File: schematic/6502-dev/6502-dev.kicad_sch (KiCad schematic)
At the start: 10 parts, among them SW1 SW_Push, U1 NE555P, U2 74HC02

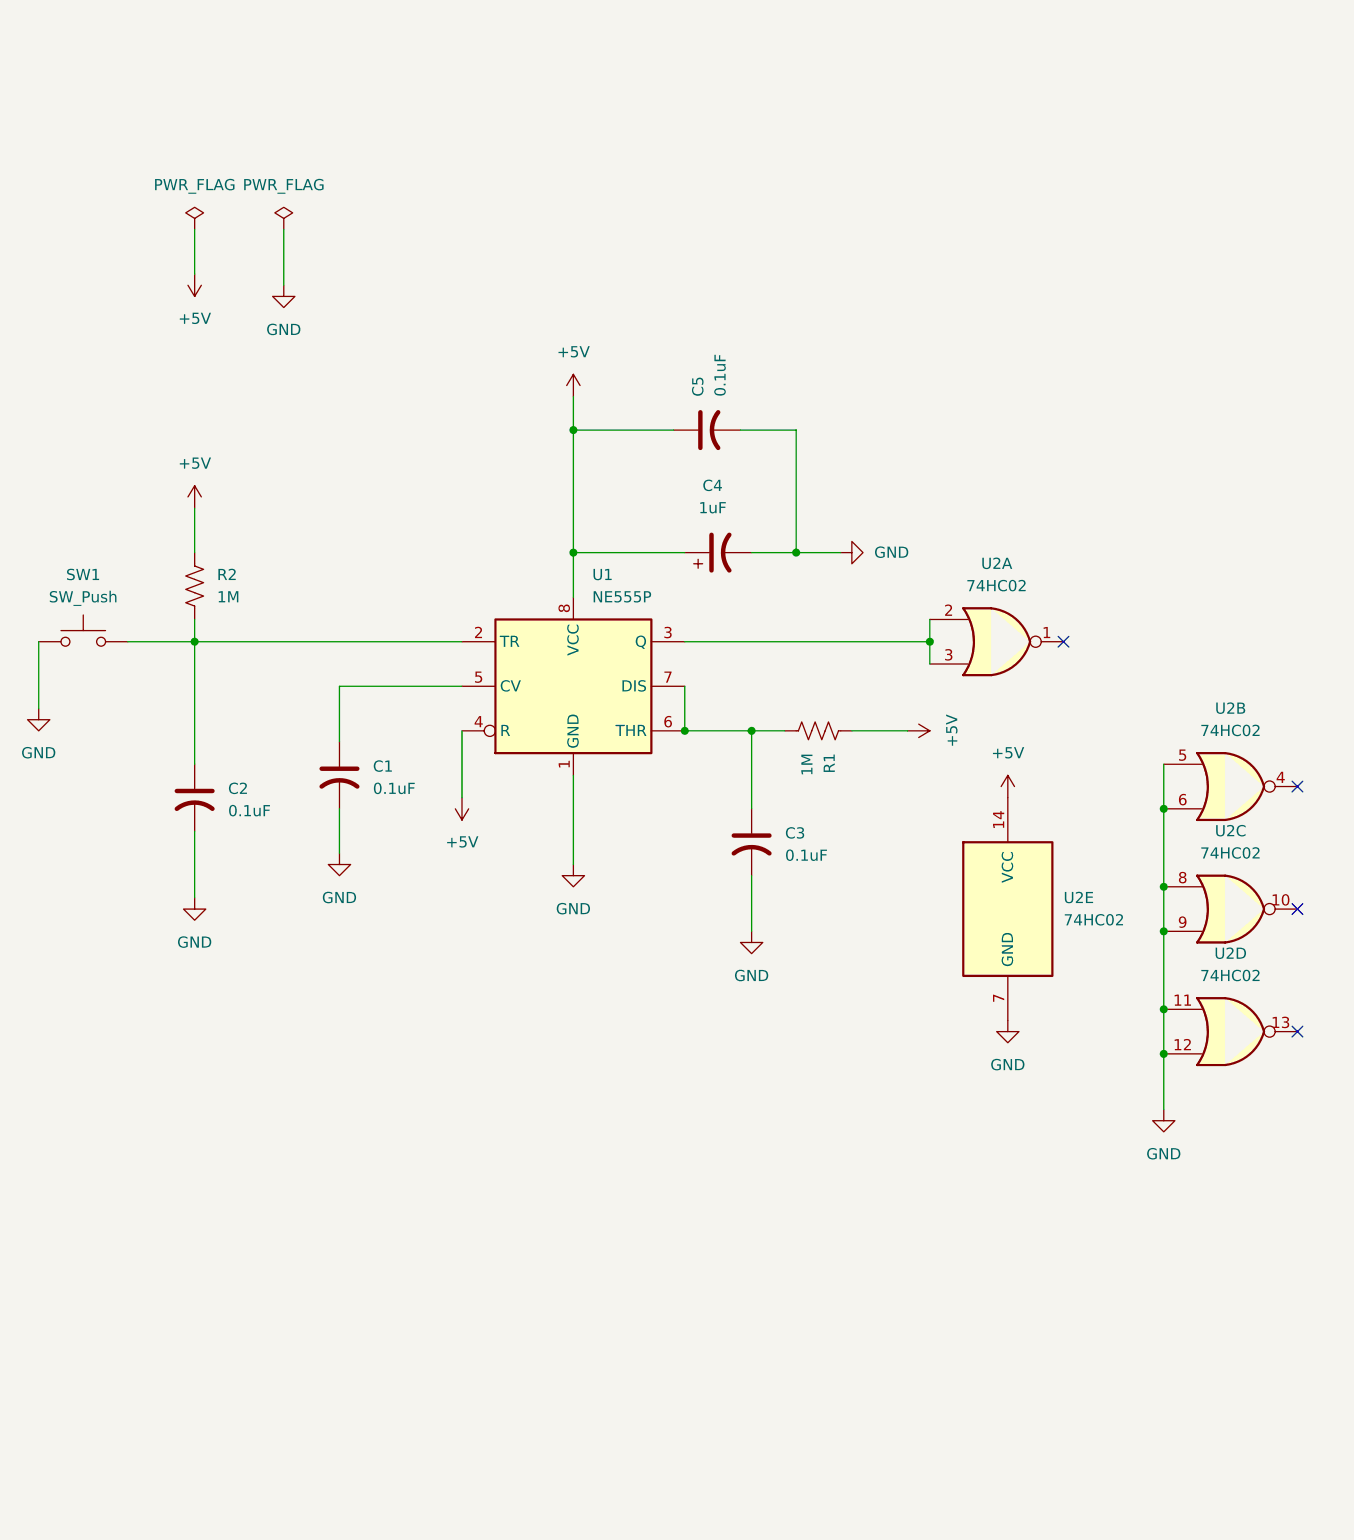
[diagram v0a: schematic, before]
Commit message: added registers as zp variables
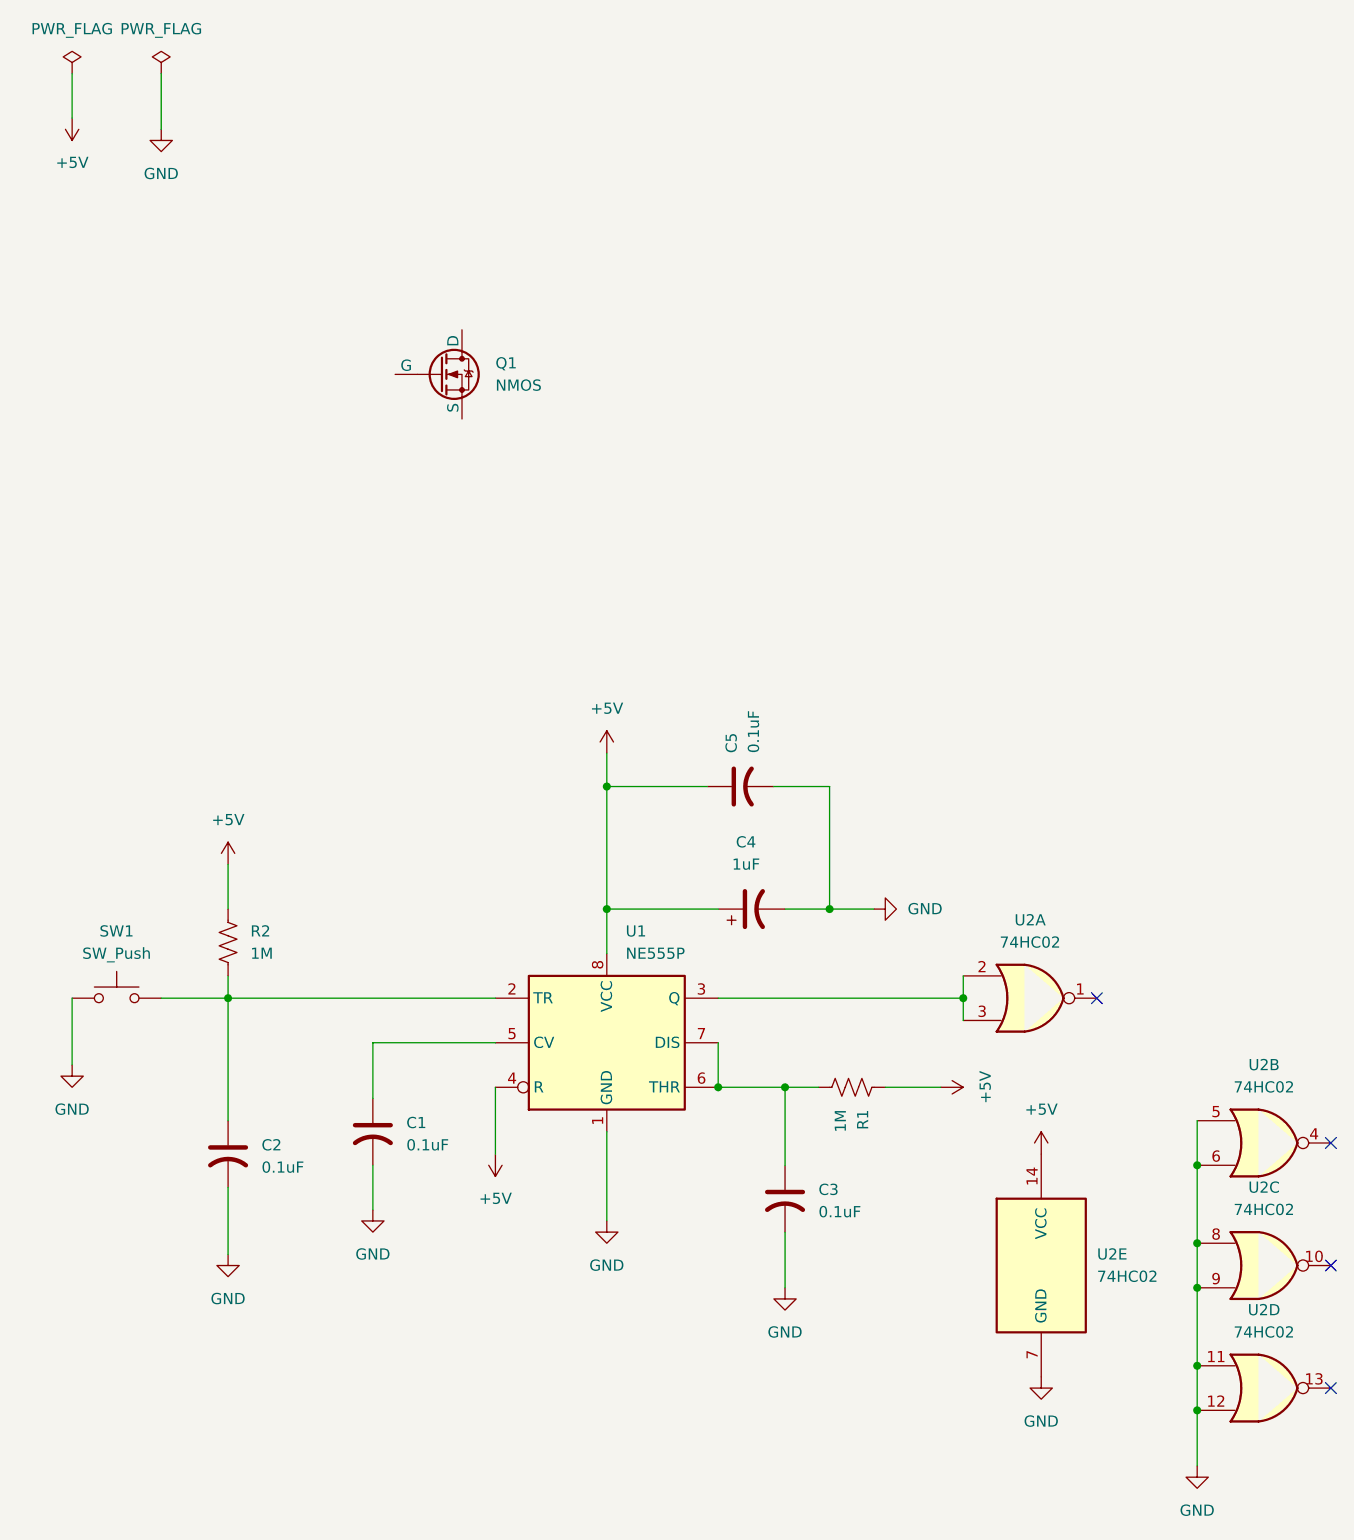
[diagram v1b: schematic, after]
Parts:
- added Q1: NMOS, symbol Simulation_SPICE:NMOS
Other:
- moved on the sheet: C1, C2, C3, C4, C5, R1, R2, SW1, U1, U2A, U2B, U2C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
